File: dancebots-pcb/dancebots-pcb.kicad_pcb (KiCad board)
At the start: 2 copper layers, 50 x 61 mm, 38 parts, among them J1 BATTERY, J2 MOT2-L, J3 MOT1-R, U1 L4941, U2 L293, U3 ATTINY261A-P, U4 LM386, U5 LM358, U6 DFR0299

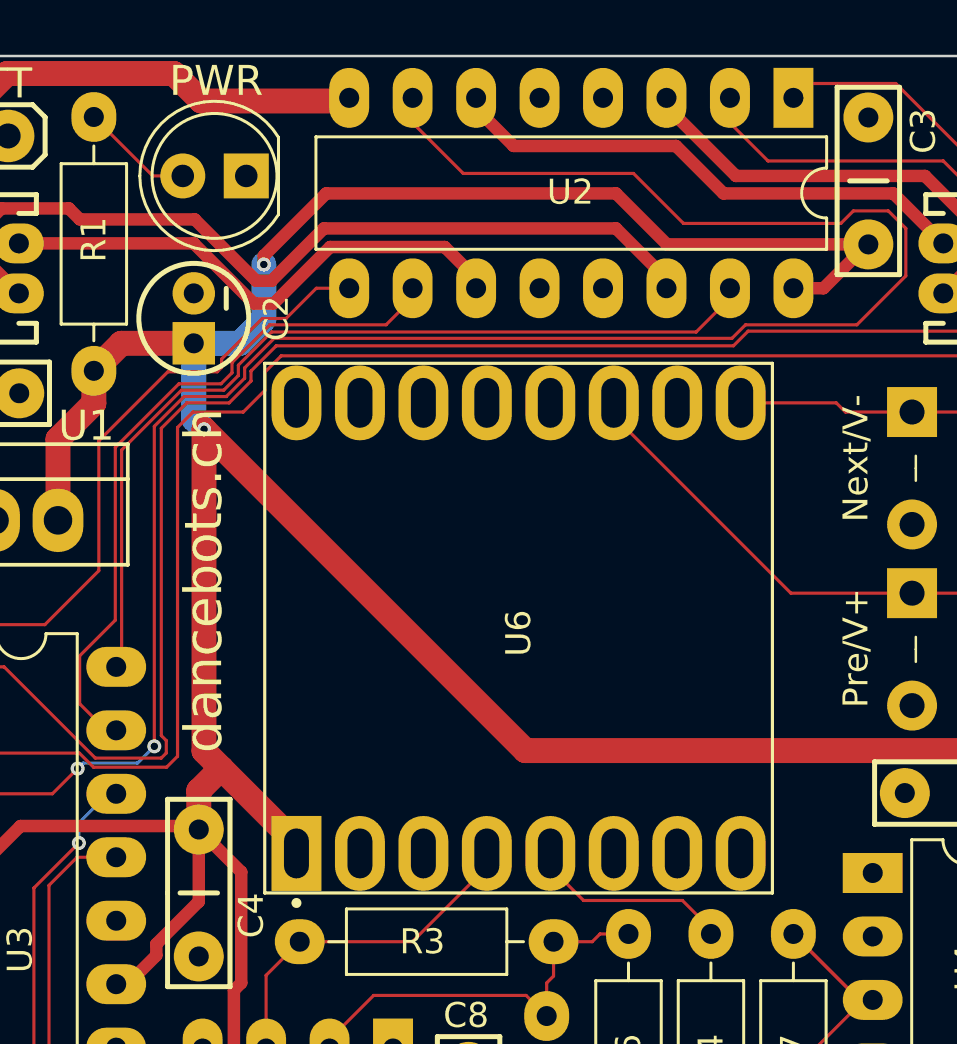
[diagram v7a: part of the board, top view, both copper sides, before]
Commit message: Version 8.2
Version 8.2
Changes on Silkscreen, polarity signs for LED, simple orientiation help for df-player. 33k instead of 20k for easier colour code Identification.
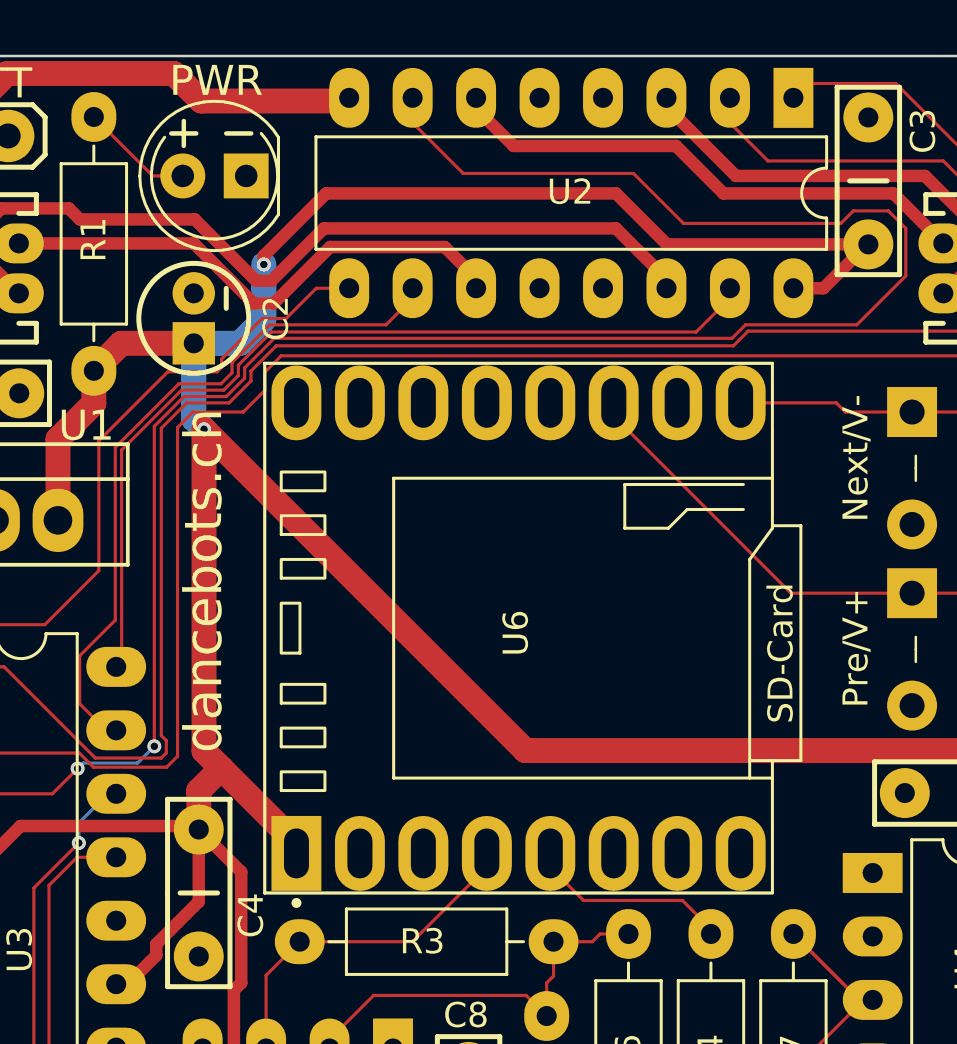
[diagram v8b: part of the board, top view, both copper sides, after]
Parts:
- R3: value 10k -> 33k
- R7: value 10k -> 1.1k
